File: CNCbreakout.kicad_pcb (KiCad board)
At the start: 2 copper layers, 147 parts, among them P101 X1, P102 X2, P103 Y, P104 Z, P105 GND, P106 +24V, P107 CONN_01X02, P108 CONN_01X02, P109 CONN_01X02, P110 Z_STOP, P111 XY_STOP, P112 VFD_IN, P113 Zaux1, P114 Zaux2, P115 Zaux3, Q201 Q_NMOS_GDS, Q202 Q_NMOS_GDS, Q203 Q_NMOS_GDS, Q204 Q_NMOS_GDS, Q205 Q_NMOS_GDS, Q206 Q_NMOS_GDS, Q301 Q_NPN_CBE, Q302 Q_NPN_CBE, Q303 Q_NPN_CBE, Q304 Q_NPN_CBE, Q305 Q_NPN_CBE, Q306 Q_NPN_CBE, Q307 Q_NPN_CBE, Q308 Q_NPN_CBE, Q309 Q_NPN_CBE, Q310 Q_NPN_CBE, Q311 Q_NPN_CBE, Q312 Q_NPN_CBE, Q313 Q_NPN_CBE, Q314 Q_NPN_CBE, Q315 Q_NPN_CBE, Q316 Q_NPN_CBE, Q317 Q_NPN_CBE, Q318 Q_NPN_CBE, U301 TCMT1108, U302 TCMT1108, U601 TCMT1108, U602 TCMT1108, U603 TCMT1108, U604 TCMT1108

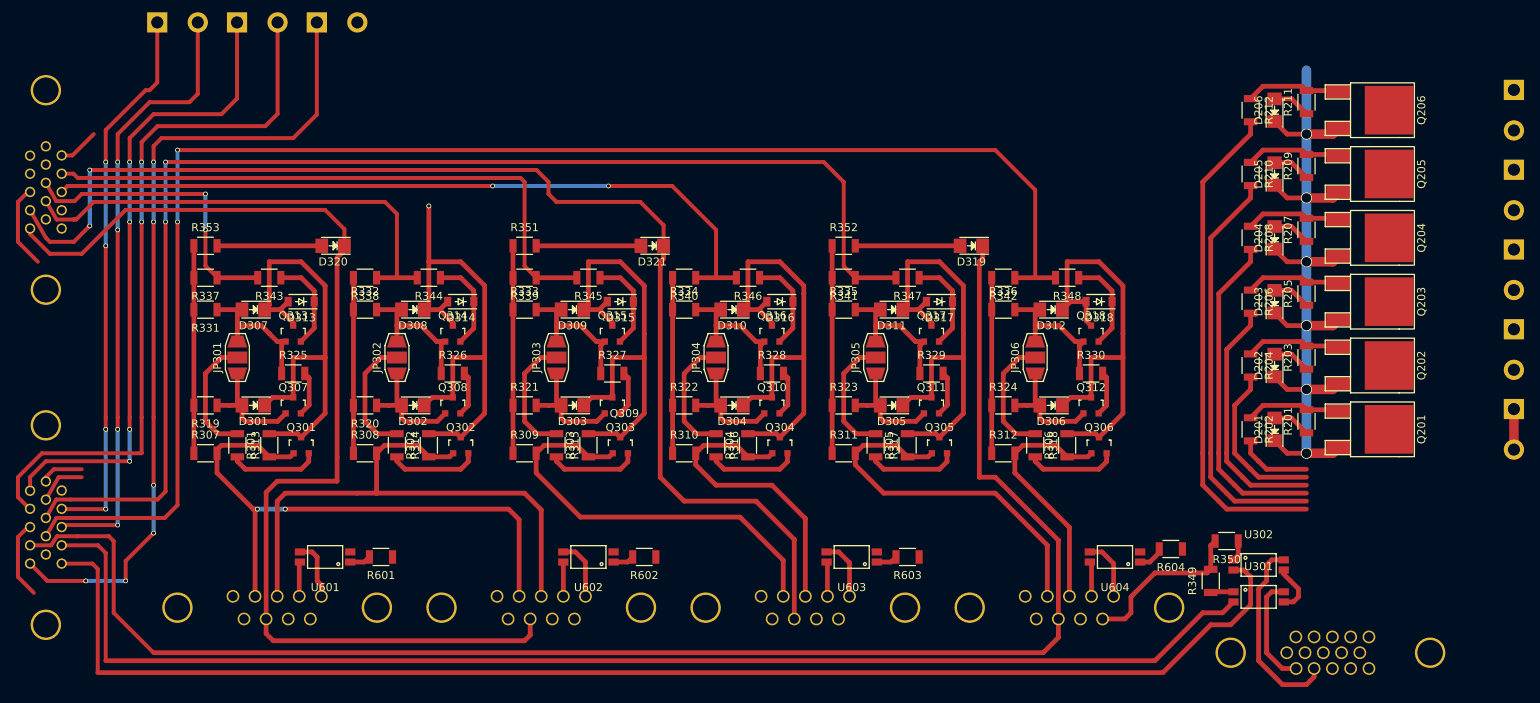
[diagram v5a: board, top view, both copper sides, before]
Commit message: added thermistor
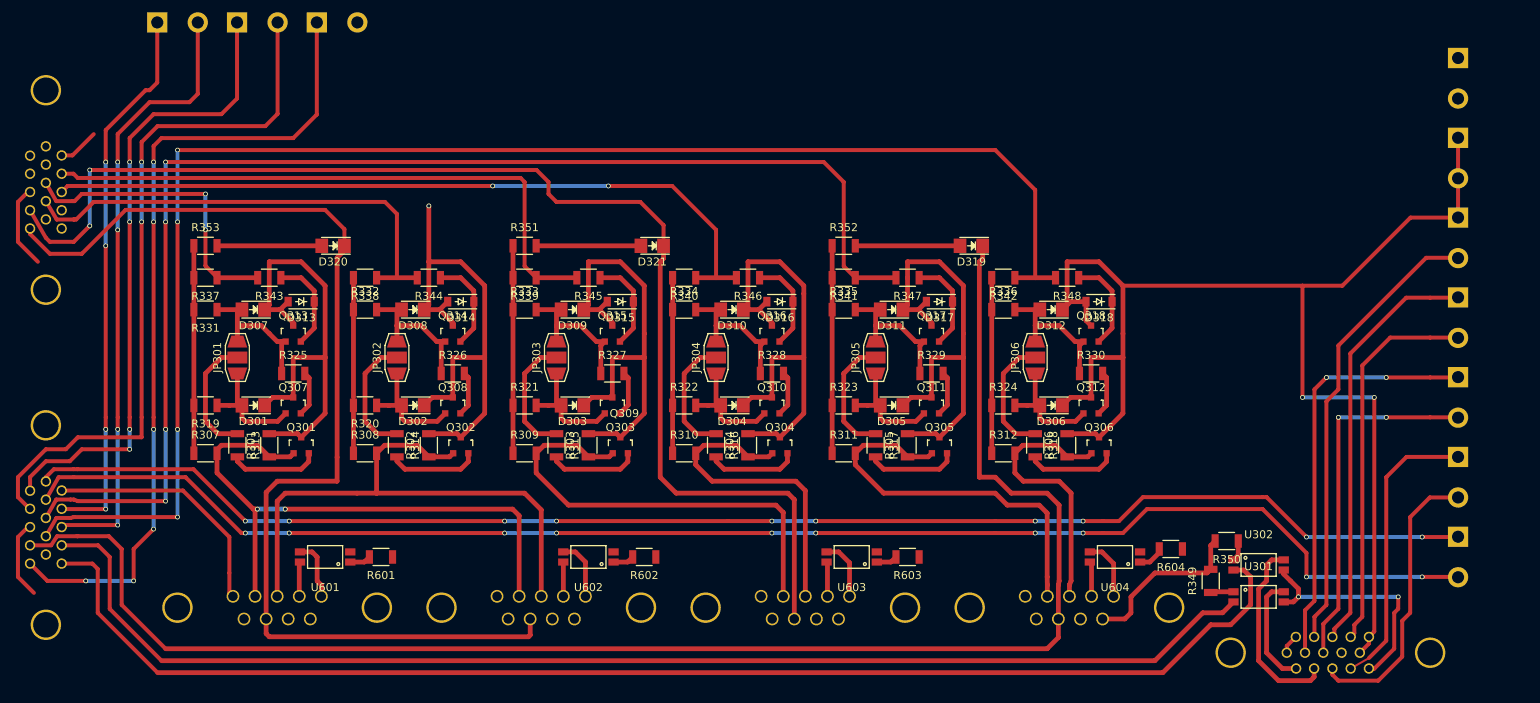
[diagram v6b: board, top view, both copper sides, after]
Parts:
- removed D201, D202, D203, D204, D205, D206: LED, LEDs:LED_1206
- removed Q201, Q202, Q203, Q204, Q205, Q206: Q_NMOS_GDS, TO_SOT_Packages_SMD:TO-252-2Lead
- removed R201, R202, R203, R204, R205, R206, R207, R208, R209, R210, R211, R212: 2K, Resistors_SMD:R_1206
- added P116: VFD_Speed, Connect:bornier2, B.Cu at (220.0, 117.0)
- added P117: VFD_Temp, Connect:bornier2, B.Cu at (220.0, 127.0)
- P107: value CONN_01X02 -> VFD_Stop
- P108: value CONN_01X02 -> VFD_FwdRev
- P109: value CONN_01X02 -> VFD_Aux
- moved P105 34.7 mm to (220.0, 77.0)
- moved P109 26.9 mm to (220.0, 107.0)
- moved P107 15.7 mm to (220.0, 87.0)
- moved P108 9.22 mm to (220.0, 97.0)
- moved P106 8.06 mm to (220.0, 67.0)
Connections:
- P107 pad 1: /vfd_aux/GPO2 -> GND
- P107 pad 2: /vfd_aux/GPO1 -> DIn_1
- P108 pad 1: /vfd_aux/GPO4 -> DIn_3
- P108 pad 2: /vfd_aux/GPO3 -> DIn_6
- P109 pad 1: /vfd_aux/GPO6 -> DIn_2
- P109 pad 2: /vfd_aux/GPO5 -> DIn_5
- P112 pad 4: DIn_5 -> DIn_6
- P112 pad 8: DIn_4 -> DIn_5
- P112 pad 9: DIn_6 -> Net-(P112-Pad9)
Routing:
- net SpindleTherm+: track 6.14 -> 188.1 mm, vias 0 -> 10
- net SpindleTherm-: track 5.44 -> 184.0 mm, vias 0 -> 10
- net DIn_1: track 9.38 -> 57.4 mm
- net DIn_4: track 41.4 -> 0.00 mm
- net LoopB: track 0.00 -> 36.3 mm
- net LoopA: track 0.00 -> 36.0 mm
- net GND: track 467.5 -> 503.1 mm, vias 7 -> 3
- net DIn_2: track 20.6 -> 52.1 mm, vias 0 -> 2
- net DGND: track 6.24 -> 29.7 mm, vias 0 -> 2
- net DIn_3: track 31.0 -> 52.9 mm
- net DIn_6: track 62.3 -> 48.1 mm
- net Net-(Q206-Pad1): track 11.9 -> 0.00 mm
- net Net-(Q205-Pad1): track 11.9 -> 0.00 mm
- net Net-(Q204-Pad1): track 11.9 -> 0.00 mm
- net Net-(Q203-Pad1): track 11.9 -> 0.00 mm
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
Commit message: full route
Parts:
- moved P113 4.50 mm to (59.5, 64.5)
- moved P114 4.50 mm to (69.5, 64.5)
- moved P115 4.50 mm to (79.5, 64.5)
- moved R601 2.55 mm to (85.5, 124.5), turned to 270 degrees
- moved R602 2.55 mm to (118.5, 124.5), turned to 270 degrees
- moved R603 2.55 mm to (151.5, 124.5), turned to 270 degrees
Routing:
- net +24V: track 187.0 -> 698.6 mm, vias 0 -> 18
- net GND: track 503.1 -> 838.2 mm, vias 3 -> 12
- net /Estop_Logic/ENABLE-: track 0.00 -> 106.4 mm, vias 0 -> 6
- net /Estop_Logic/ENABLE+: track 0.00 -> 103.1 mm, vias 0 -> 6
- net F1_LIM: track 74.6 -> 81.1 mm
- net SOL2: track 77.2 -> 72.7 mm
- net SOL1: track 69.5 -> 65.0 mm
- net Net-(P110-Pad12): track 89.2 -> 84.7 mm
- net Net-(P110-Pad11): track 79.7 -> 75.2 mm
- net LimY-: track 95.7 -> 99.7 mm
- net HomeY: track 157.9 -> 161.7 mm, vias 2 -> 4
- net LimX-: track 59.9 -> 63.7 mm, vias 0 -> 2
- net Net-(P110-Pad15): track 103.1 -> 99.4 mm
- net LoopA: track 36.0 -> 39.0 mm
- net HomeX: track 138.9 -> 141.5 mm, vias 0 -> 2
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
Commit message: added enable input connector
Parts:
- added P118: Enable, Connect:bornier2, B.Cu at (185.0, 65.0)
- moved D301 0.71 mm to (69.5, 108.5)
- moved D302 0.71 mm to (89.5, 108.5)
- moved D303 0.71 mm to (109.5, 108.5)
- moved D304 0.71 mm to (129.5, 108.5)
- moved D305 0.71 mm to (149.5, 108.5)
- moved D306 0.71 mm to (169.5, 108.5)
- moved D307 0.71 mm to (69.5, 96.5)
- moved D308 0.71 mm to (89.5, 96.5)
- moved D309 0.71 mm to (109.5, 96.5)
- moved D310 0.71 mm to (129.5, 96.5)
- moved D311 0.71 mm to (149.5, 96.5)
- moved D312 0.71 mm to (169.5, 96.5)
- moved D313 0.71 mm to (75.5, 95.5)
- moved D314 0.71 mm to (95.5, 95.5)
- moved D315 0.71 mm to (115.5, 95.5)
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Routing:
- net /Estop_Logic/ENABLE+: track 103.1 -> 168.6 mm, vias 6 -> 8
- net /Estop_Logic/ENABLE-: track 106.4 -> 171.6 mm, vias 6 -> 8
- net +24V: track 698.6 -> 677.8 mm
- net SpindleTherm-: track 182.3 -> 181.8 mm
- net SpindleTherm+: track 186.1 -> 185.6 mm
- net LoopB: track 36.3 -> 35.8 mm
- net LoopA: track 39.0 -> 38.5 mm
- net GND: track 838.2 -> 837.7 mm
- net DIn_6: track 48.1 -> 47.6 mm
- net DIn_5: track 44.1 -> 43.6 mm
- net DIn_3: track 52.9 -> 52.4 mm
- net DIn_2: track 51.2 -> 50.7 mm
- net DIn_1: track 57.4 -> 56.9 mm
